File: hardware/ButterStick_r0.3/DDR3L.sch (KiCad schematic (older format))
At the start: 2 parts, among them U4 MT41K64M16TW-107_J-TR

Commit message: hw.r0_3: cleanup and additions
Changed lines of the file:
@@
 $Descr A4 11693 8268
 encoding utf-8
-Sheet 6 16
+Sheet 14 20
 Title ""
 Date ""
@@
 	3300 6100 6500 6100
 Wire Bus Line
-	4350 2200 4350 2500
-Wire Bus Line
-	4350 2500 4350 2700
-Wire Bus Line
-	4350 2700 4350 2900
-Wire Bus Line
-	4350 2900 4350 3100
-Wire Bus Line
-	4350 3100 4350 3300
-Wire Bus Line
-	4350 3300 4350 3500
-Wire Bus Line
-	4350 3500 4350 3700
-Wire Bus Line
-	4350 3700 4350 3900
-Wire Bus Line
-	4350 3900 4350 4200
-Wire Bus Line
-	4350 4200 4350 4400
-Wire Bus Line
-	4350 4400 4350 4700
-Wire Bus Line
-	4350 4700 4350 4900
+	4350 2200 4350 2600
+Wire Bus Line
+	4350 2600 4350 2800
+Wire Bus Line
+	4350 2800 4350 3000
+Wire Bus Line
+	4350 3000 4350 3200
+Wire Bus Line
+	4350 3200 4350 3400
+Wire Bus Line
+	4350 3400 4350 3600
+Wire Bus Line
+	4350 3600 4350 3800
+Wire Bus Line
+	4350 3800 4350 4000
+Wire Bus Line
+	4350 4000 4350 4300
+Wire Bus Line
+	4350 4300 4350 4600
+Wire Bus Line
+	4350 4600 4350 4800
+Wire Bus Line
+	4350 4800 4350 4900
 Wire Bus Line
 	4350 4900 4350 5100
@@
 	4350 5100 4350 5400
 Wire Bus Line
-	4350 5400 4350 5600
-Wire Bus Line
-	4350 5600 4350 5700
-Wire Bus Line
-	6500 3550 6500 3650
-Wire Bus Line
-	6500 3650 6500 3850
-Wire Bus Line
-	6500 3850 6500 3950
+	4350 5400 4350 5500
+Wire Bus Line
+	4350 5500 4350 5700
+Wire Bus Line
+	6500 3550 6500 3750
+Wire Bus Line
+	6500 3750 6500 3950
 Wire Bus Line
 	6500 3950 6500 4150
@@
 	6500 4150 6500 4450
 Wire Bus Line
-	6500 4450 6500 4550
-Wire Bus Line
-	6500 4550 6500 4750
-Wire Bus Line
-	6500 4750 6500 4850
+	6500 4450 6500 4650
+Wire Bus Line
+	6500 4650 6500 4850
 Wire Bus Line
 	6500 4850 6500 5050
 Wire Bus Line
-	6500 5050 6500 5550
-Wire Bus Line
-	6500 5550 6500 5800
-Wire Bus Line
-	6500 5800 6500 6100
+	6500 5050 6500 5150
+Wire Bus Line
+	6500 5150 6500 5650
+Wire Bus Line
+	6500 5650 6500 5900
+Wire Bus Line
+	6500 5900 6500 6100
 Text Label 3950 2200 2    50   ~ 0
 {DRAM_CTRL}

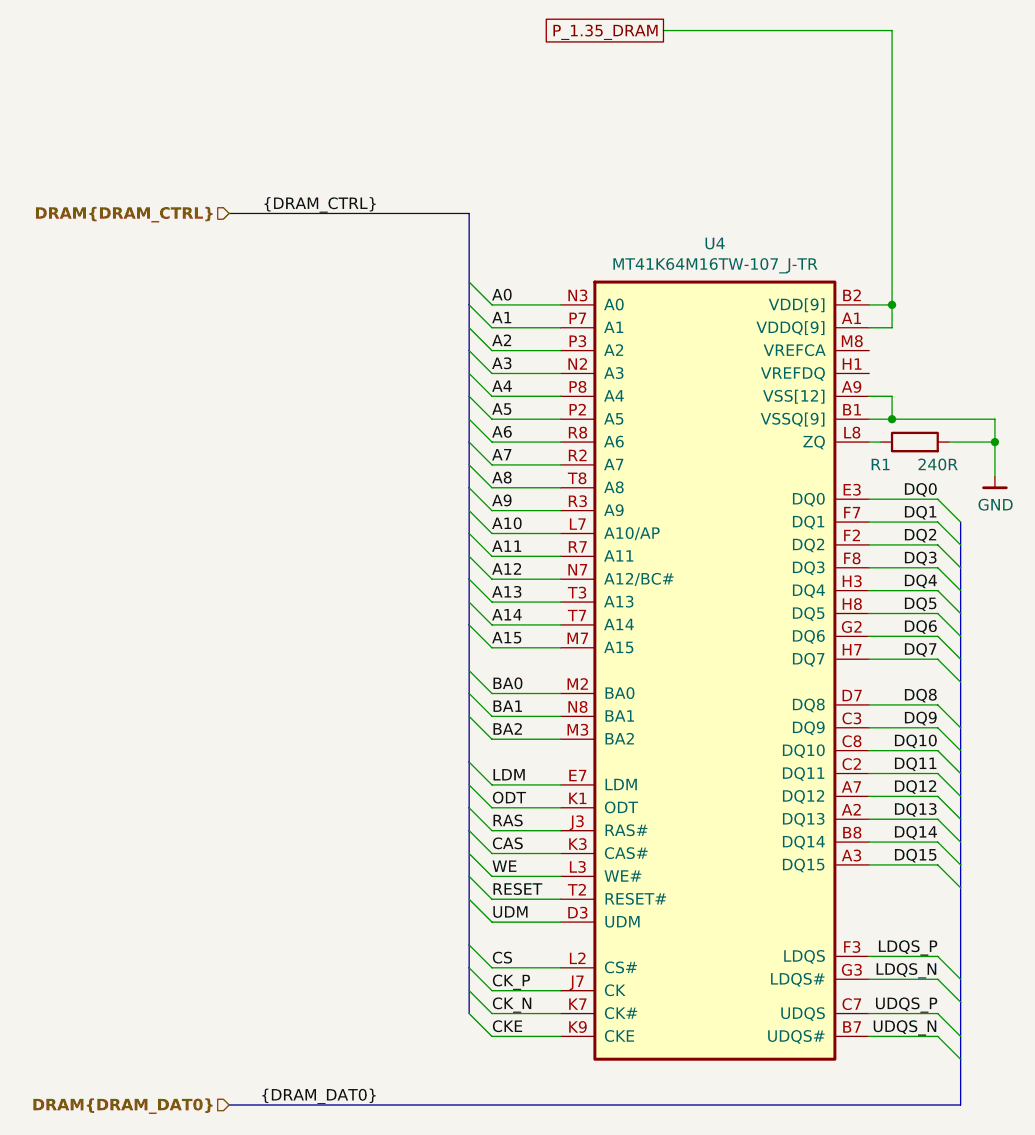
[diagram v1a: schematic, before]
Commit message: hw.r0_3: Update schematics with 85F-5G symbol
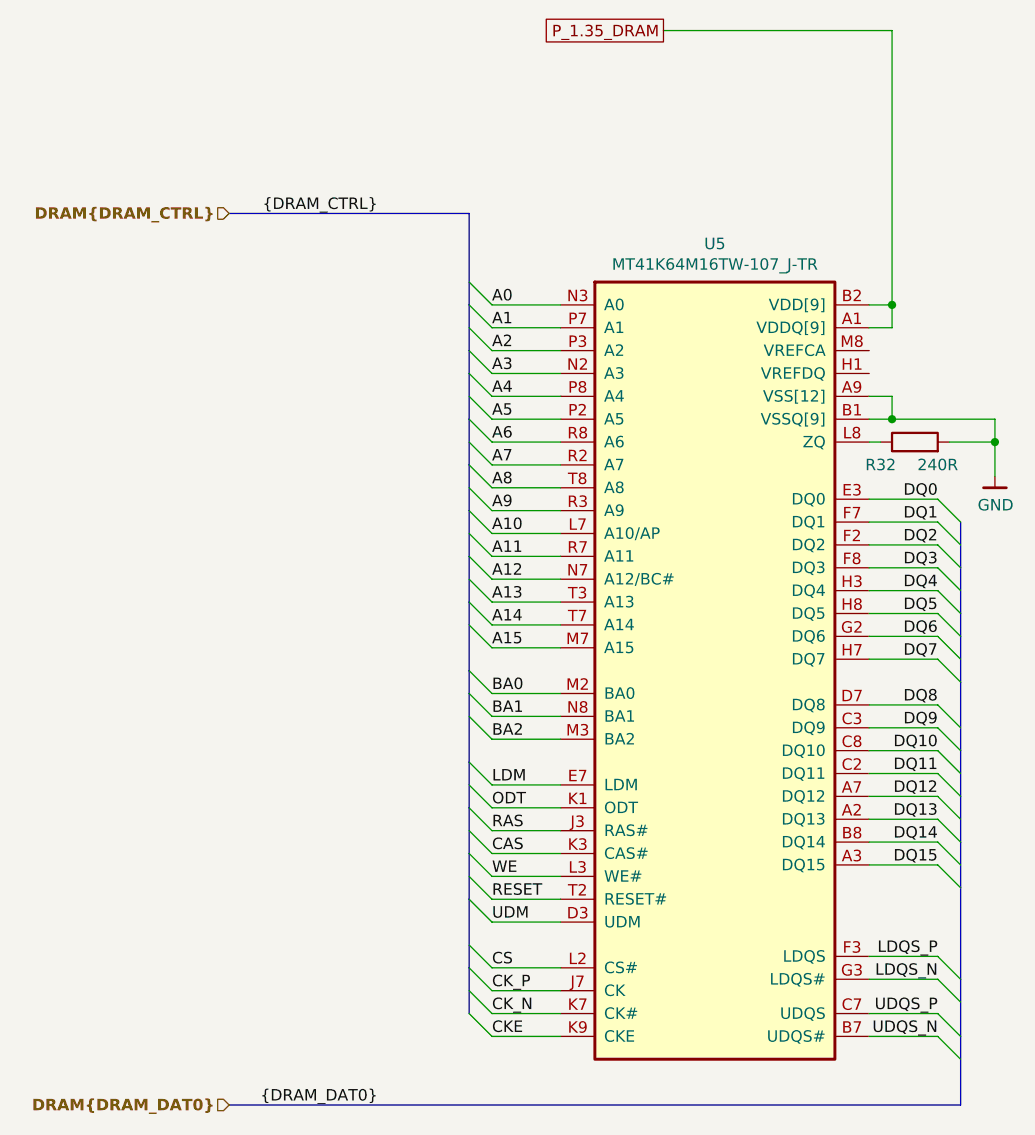
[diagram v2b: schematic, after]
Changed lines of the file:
@@
 $Descr A4 11693 8268
 encoding utf-8
-Sheet 14 20
+Sheet 3 18
 Title ""
 Date ""
@@
 	4350 2600 4350 2800
 Wire Bus Line
-	4350 2800 4350 3000
-Wire Bus Line
-	4350 3000 4350 3200
-Wire Bus Line
-	4350 3200 4350 3400
-Wire Bus Line
-	4350 3400 4350 3600
-Wire Bus Line
-	4350 3600 4350 3800
-Wire Bus Line
-	4350 3800 4350 4000
-Wire Bus Line
-	4350 4000 4350 4300
+	4350 2800 4350 2900
+Wire Bus Line
+	4350 2900 4350 3100
+Wire Bus Line
+	4350 3100 4350 3300
+Wire Bus Line
+	4350 3300 4350 3500
+Wire Bus Line
+	4350 3500 4350 3700
+Wire Bus Line
+	4350 3700 4350 3900
+Wire Bus Line
+	4350 3900 4350 4200
+Wire Bus Line
+	4350 4200 4350 4300
 Wire Bus Line
 	4350 4300 4350 4600
@@
 	4350 4600 4350 4800
 Wire Bus Line
-	4350 4800 4350 4900
-Wire Bus Line
-	4350 4900 4350 5100
-Wire Bus Line
-	4350 5100 4350 5400
-Wire Bus Line
-	4350 5400 4350 5500
+	4350 4800 4350 5000
+Wire Bus Line
+	4350 5000 4350 5200
+Wire Bus Line
+	4350 5200 4350 5500
 Wire Bus Line
 	4350 5500 4350 5700
@@
 	6500 3750 6500 3950
 Wire Bus Line
-	6500 3950 6500 4150
-Wire Bus Line
-	6500 4150 6500 4450
-Wire Bus Line
-	6500 4450 6500 4650
-Wire Bus Line
-	6500 4650 6500 4850
-Wire Bus Line
-	6500 4850 6500 5050
-Wire Bus Line
-	6500 5050 6500 5150
-Wire Bus Line
-	6500 5150 6500 5650
-Wire Bus Line
-	6500 5650 6500 5900
-Wire Bus Line
-	6500 5900 6500 6100
+	6500 3950 6500 4050
+Wire Bus Line
+	6500 4050 6500 4250
+Wire Bus Line
+	6500 4250 6500 4550
+Wire Bus Line
+	6500 4550 6500 4750
+Wire Bus Line
+	6500 4750 6500 4950
+Wire Bus Line
+	6500 4950 6500 5150
+Wire Bus Line
+	6500 5150 6500 5550
+Wire Bus Line
+	6500 5550 6500 5800
+Wire Bus Line
+	6500 5800 6500 6100
 Text Label 3950 2200 2    50   ~ 0
 {DRAM_CTRL}
@@
 AR Path="/5ABD38F2/5EB207D6/5E919612" Ref="#PWR0108"  Part="1"
 AR Path="/5ABD38F2/5EB15CF3/5E919612" Ref="#PWR0224"  Part="1"
-F 0 "#PWR0224" H 6650 3100 50  0001 C CNN
+F 0 "#PWR0108" H 6650 3100 50  0001 C CNN
 F 1 "GND" H 6653 3224 50  0000 C CNN
 F 2 "" H 6550 3000 50  0001 C CNN
@@
 AR Path="/5EB207D6/5E915DBF" Ref="R1"  Part="1"
 AR Path="/5ABD38F2/5EB207D6/5E915DBF" Ref="R32"  Part="1"
-F 0 "R1" V 6200 3350 50  0000 C CNN
+F 0 "R32" V 6200 3350 50  0000 C CNN
 F 1 "240R" V 6200 3100 50  0000 C CNN
 F 2 "" V 6230 3200 50  0001 C CNN
@@
 AR Path="/5EB207D6/5E57D9A3" Ref="U4"  Part="1"
 AR Path="/5ABD38F2/5EB207D6/5E57D9A3" Ref="U5"  Part="1"
-F 0 "U4" H 5425 5267 50  0000 C CNN
+F 0 "U5" H 5425 5267 50  0000 C CNN
 F 1 "MT41K64M16TW-107_J-TR" H 5425 5177 50  0000 C CNN
 F 2 "Package_BGA:BGA-96_9.0x13.0mm_Layout2x3x16_P0.8mm" H 5450 5300 50  0001 C CNN

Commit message: hw.r0_3: Start pin assignments for DDR3
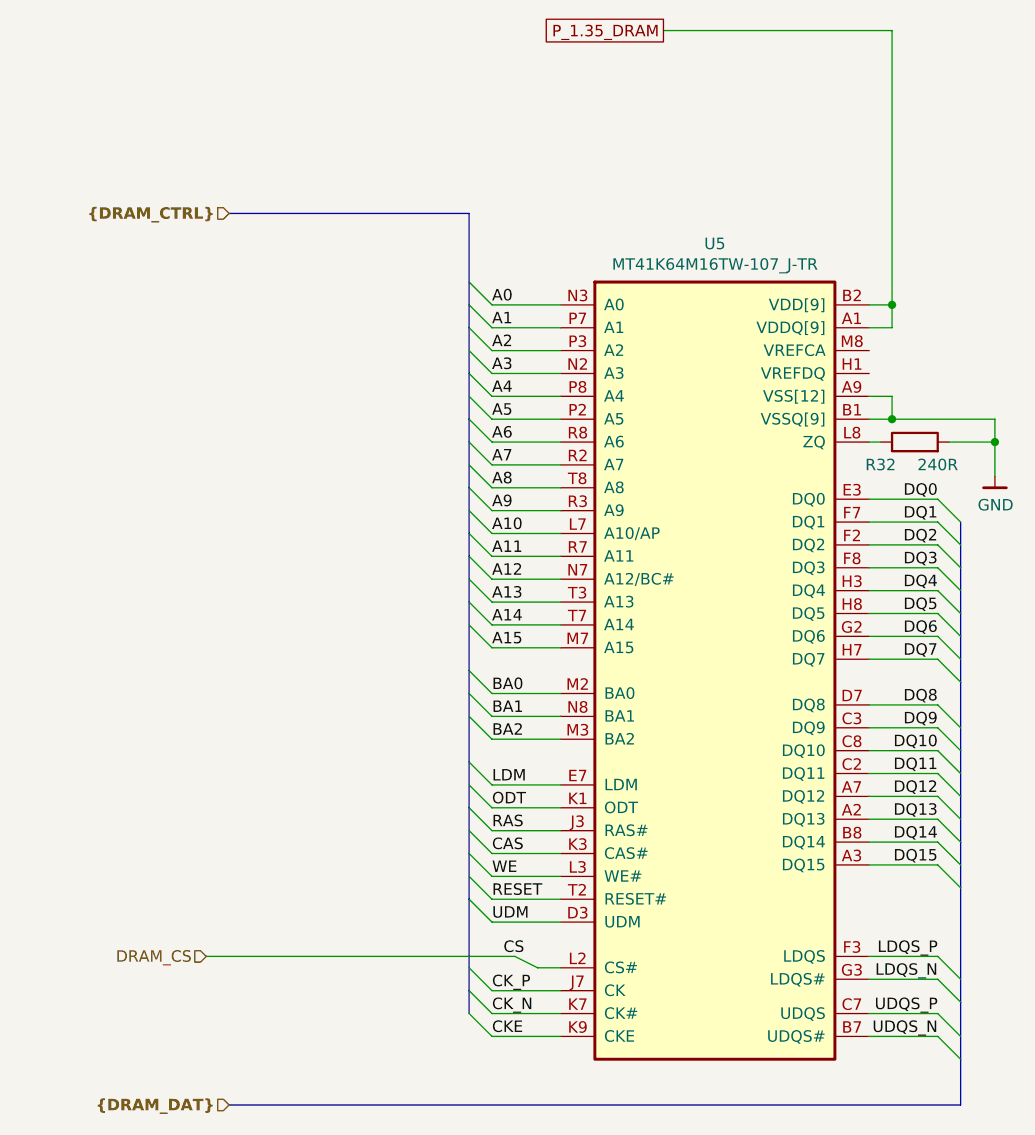
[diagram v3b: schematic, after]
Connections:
- net CS renamed DRAM_CS
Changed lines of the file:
@@
 $Descr A4 11693 8268
 encoding utf-8
-Sheet 3 18
+Sheet 15 20
 Title ""
 Date ""
@@
 	4350 5200 4450 5300
 Entry Wire Line
-	4350 5400 4450 5500
-Entry Wire Line
 	4350 5500 4450 5600
 Entry Wire Line
@@
 	6500 5900 6400 5800
 Wire Wire Line
+	3200 5450 4550 5450
+Wire Wire Line
 	4450 2600 4750 2600
 Wire Wire Line
@@
 	4450 5300 4750 5300
 Wire Wire Line
-	4450 5500 4750 5500
-Wire Wire Line
 	4450 5600 4750 5600
 Wire Wire Line
@@
 	4450 5800 4750 5800
 Wire Wire Line
+	4550 5450 4650 5500
+Wire Wire Line
+	4650 5500 4750 5500
+Wire Wire Line
 	6100 2600 6200 2600
 Wire Wire Line
@@
 	4350 2200 4350 2600
 Wire Bus Line
-	4350 2600 4350 2800
-Wire Bus Line
-	4350 2800 4350 2900
+	4350 2600 4350 2700
+Wire Bus Line
+	4350 2700 4350 2900
 Wire Bus Line
 	4350 2900 4350 3100
 Wire Bus Line
-	4350 3100 4350 3300
-Wire Bus Line
-	4350 3300 4350 3500
-Wire Bus Line
-	4350 3500 4350 3700
+	4350 3100 4350 3200
+Wire Bus Line
+	4350 3200 4350 3400
+Wire Bus Line
+	4350 3400 4350 3600
+Wire Bus Line
+	4350 3600 4350 3700
 Wire Bus Line
 	4350 3700 4350 3900
@@
 	4350 5000 4350 5200
 Wire Bus Line
-	4350 5200 4350 5500
-Wire Bus Line
-	4350 5500 4350 5700
+	4350 5200 4350 5600
+Wire Bus Line
+	4350 5600 4350 5700
 Wire Bus Line
 	6500 3550 6500 3750
@@
 	6500 4950 6500 5150
 Wire Bus Line
-	6500 5150 6500 5550
-Wire Bus Line
-	6500 5550 6500 5800
-Wire Bus Line
-	6500 5800 6500 6100
-Text Label 3950 2200 2    50   ~ 0
-{DRAM_CTRL}
-Text Label 3950 6100 2    50   ~ 0
-{DRAM_DAT0}
+	6500 5150 6500 5650
+Wire Bus Line
+	6500 5650 6500 5900
+Wire Bus Line
+	6500 5900 6500 6100
 Text Label 4450 2600 0    50   ~ 0
 A0
@@
 Text Label 4450 5300 0    50   ~ 0
 UDM
-Text Label 4450 5500 0    50   ~ 0
-CS
 Text Label 4450 5600 0    50   ~ 0
 CK_P
@@
 Text Label 4450 5800 0    50   ~ 0
 CKE
+Text Label 4500 5450 0    50   ~ 0
+CS
 Text Label 6400 3450 2    50   ~ 0
 DQ0
@@
 Text GLabel 5200 1400 0    50   UnSpc ~ 0
 P_1.35_DRAM
+Text HLabel 3200 5450 0    50   Input ~ 0
+DRAM_CS
 Text HLabel 3300 2200 0    50   Input ~ 10
-DRAM{DRAM_CTRL}
+{DRAM_CTRL}
 Text HLabel 3300 6100 0    50   Input ~ 10
-DRAM{DRAM_DAT0}
+{DRAM_DAT}
 $Comp
 L power:GND #PWR0108
